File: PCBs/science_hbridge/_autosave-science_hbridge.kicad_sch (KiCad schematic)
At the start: 34 parts, among them J1 Conn_02x07_Odd_Even, J2 Conn_02x08_Odd_Even, J3 Conn_02x08_Odd_Even, J4 Conn_01x06, J6 Conn_01x02_Pin, J7 Conn_01x04_Pin, J8 Conn_01x06, U1 L298N, U2 MAX485E, U3 NCP718xSN500

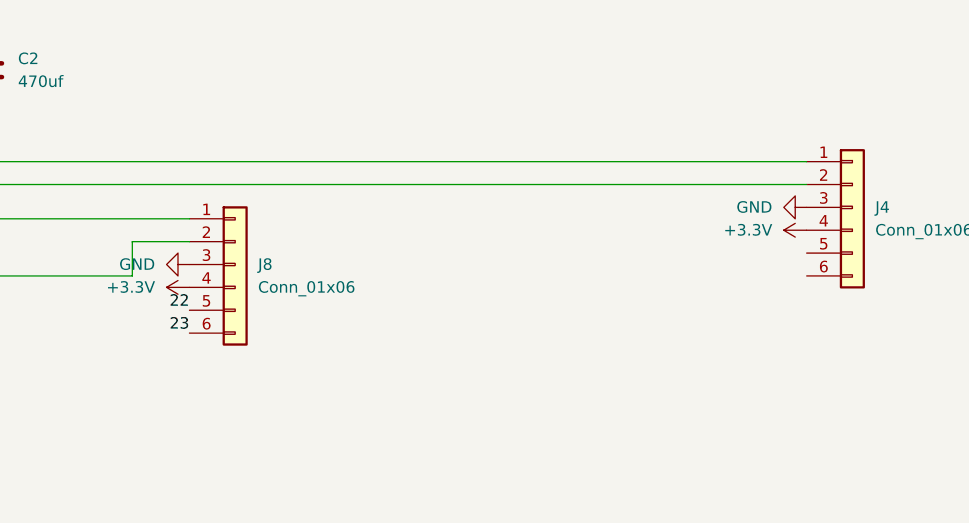
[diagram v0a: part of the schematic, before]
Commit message: added quadrature and mounting holes
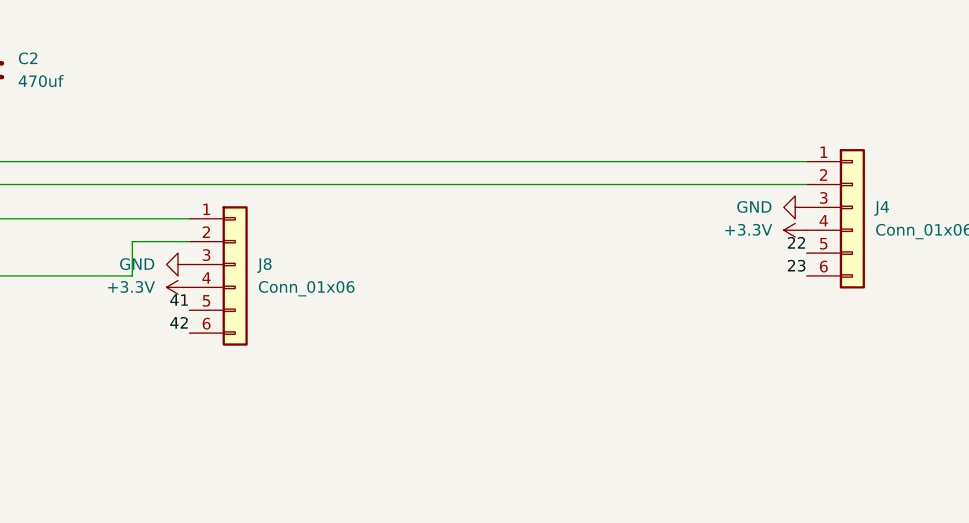
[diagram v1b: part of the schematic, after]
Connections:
- net 22: now also J4.5 (Pin_5); no longer J8.5 (Pin_5)
- net 23: now also J4.6 (Pin_6); no longer J8.6 (Pin_6)
- net 41: now also J8.5 (Pin_5)
- net 42: now also J8.6 (Pin_6)
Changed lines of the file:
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@@
+		)
+	)
+	(label "23"
+		(at 472.44 193.04 180)
+		(effects
+			(font
+				(size 1.27 1.27)
+			)
+			(justify right bottom)
 		)
 	)
@@
 		)
 	)
+	(label "41"
+		(at 403.86 196.85 180)
+		(effects
+			(font
+				(size 1.27 1.27)
+			)
+			(justify right bottom)
+		)
+	)
 	(label "22"
-		(at 403.86 196.85 180)
+		(at 472.44 190.5 180)
 		(effects
 			(font
@@
 		)
 	)
-	(label "23"
+	(label "42"
 		(at 403.86 199.39 180)
 		(effects
